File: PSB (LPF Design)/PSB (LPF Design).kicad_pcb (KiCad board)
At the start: 2 copper layers, 78 x 50 mm, 18 parts, among them J1 Screw_Terminal_01x02, U1 TL081, U2 TL081

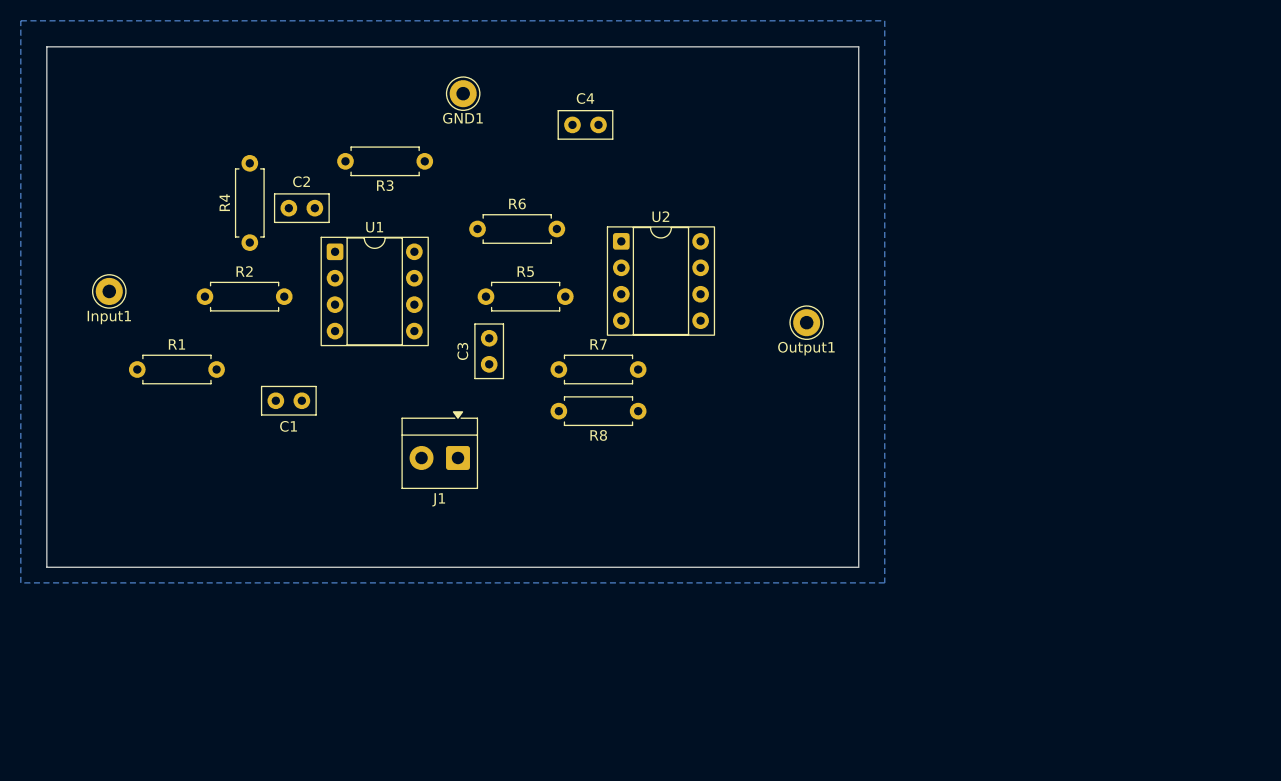
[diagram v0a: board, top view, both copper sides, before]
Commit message: third revision(forgot the resistor)
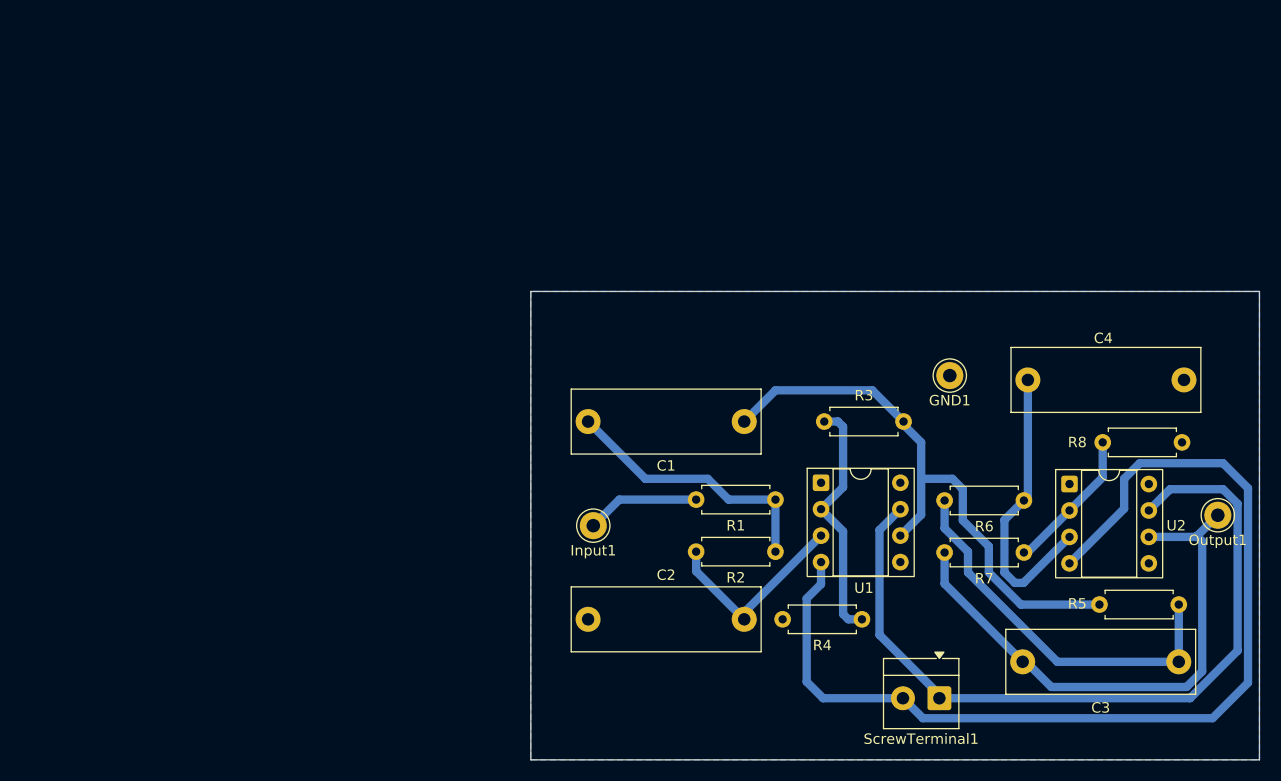
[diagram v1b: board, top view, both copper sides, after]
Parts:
- C1, C2, C3, C4: footprint Capacitor_THT:C_Disc_D5.0mm_W2.5mm_P2.50mm -> Capacitor_THT:C_Rect_L18.0mm_W6.0mm_P15.00mm_FKS3_FKP3
- moved R4 69.1 mm to (168.8, 103.5), turned to 180 degrees
- moved R5 65.9 mm to (191.6, 102.1)
- moved C4 63.7 mm to (199.8, 80.5), turned to 180 degrees
- moved R2 60.0 mm to (160.5, 97.0), turned to 180 degrees
- moved C3 58.7 mm to (184.2, 107.6), turned to 0 degrees
- moved R1 55.1 mm to (152.9, 92.0)
- moved GND1 54.0 mm to (177.2, 80.1)
- moved R3 52.4 mm to (172.8, 84.5)
- moved R6 51.9 mm to (176.8, 92.1)
- moved U1 51.7 mm to (164.9, 90.4)
- moved ScrewTerminal1 51.7 mm to (176.2, 111.1)
- moved Input1 51.7 mm to (143.0, 94.5)
- moved U2 49.0 mm to (188.8, 90.5)
- moved C2 48.9 mm to (142.5, 103.5)
- moved R8 44.7 mm to (191.9, 86.5), turned to 0 degrees
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- renumbered J1 to ScrewTerminal1
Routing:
- net V-: track 0.00 -> 99.8 mm
- net V+: track 0.00 -> 76.0 mm
- net Net-(C1-Pad1): track 0.00 -> 55.6 mm
- net Net-(C3-Pad1): track 0.00 -> 53.2 mm
- net Net-(C3-Pad2): track 0.00 -> 37.2 mm
- net Net-(U2-+): track 0.00 -> 27.9 mm
- net Net-(C1-Pad2): track 0.00 -> 26.1 mm
- net Net-(U1--): track 0.00 -> 23.8 mm
- net Net-(U1-+): track 0.00 -> 19.5 mm
- net Net-(U2--): track 0.00 -> 13.9 mm
- net Net-(Input1-Pad1): track 0.00 -> 10.9 mm
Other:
- board size 78 x 50 mm -> 70 x 45 mm
